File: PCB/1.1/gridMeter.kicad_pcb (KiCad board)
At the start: 2 copper layers, 50 x 50 mm, 26 parts, among them CON1 AC POWER, IC1 ATTINY84A-SS, P2 AC POWER, P3 MOTOR, P4 ISP, U1 LE33CZ-TR, U2 TCXO_SMD_4P, U3 TCRT5000, U4 7805, U5 ULN2003

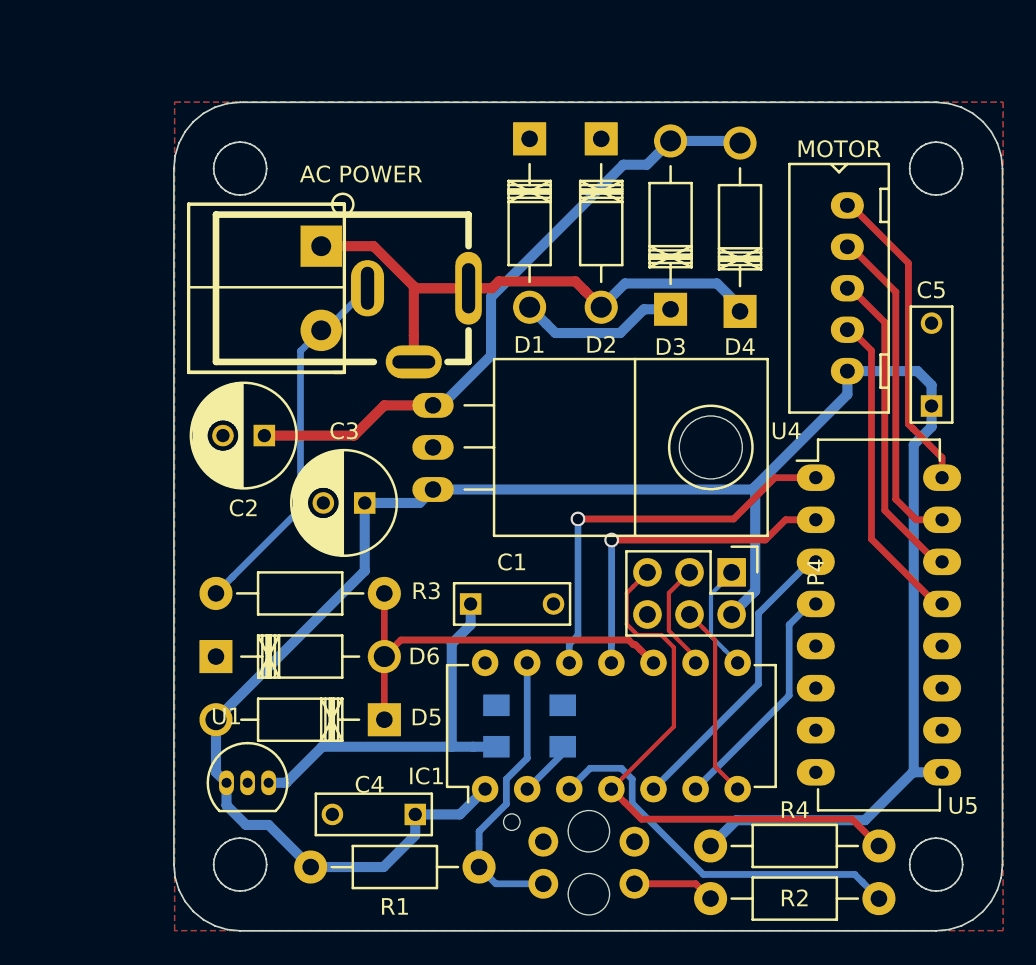
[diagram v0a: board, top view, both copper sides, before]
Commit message: Changes to Schematic PCB Gerbers
Matt Little changes to components - added different values and suppliers
codes. Slight change to PCB and footprints. Added Logo to silkscreen.
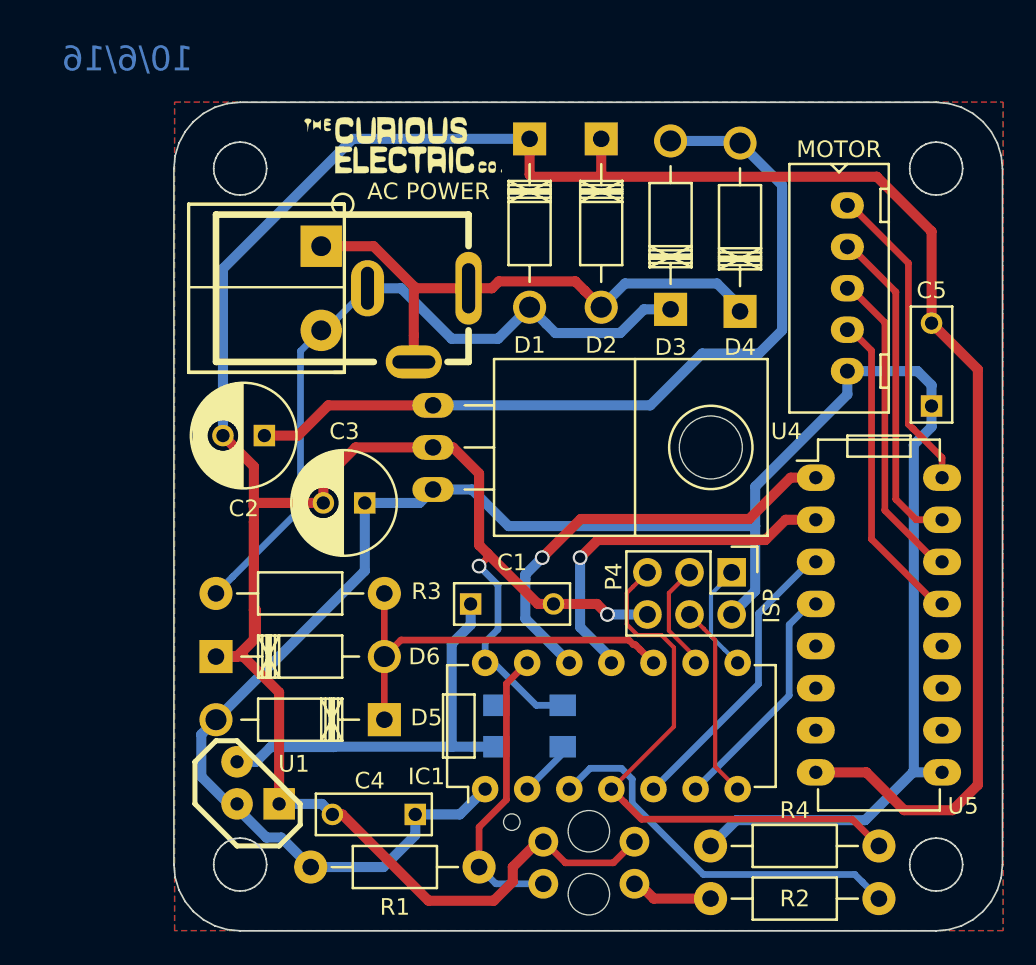
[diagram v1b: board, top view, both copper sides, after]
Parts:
- added P6: LOGO1, CuriousElectric2:CuriousElectric_flat_12mm, F.Cu at (193.7, 122.6)
- IC1: value ATTINY84A-SS -> ATTINY84A-PU; footprint Housings_DIP:DIP-14_W7.62mm -> DIP-14_W7.62mm
- U1: value LE33CZ-TR -> MCP170-3_3V; footprint TO_SOT_Packages_THT:TO-92_Inline_Narrow_Oval -> matts_components:TO92-MCP1700
- U5: footprint Housings_DIP:DIP-16_W7.62mm_LongPads -> DIP-16_W7.62mm_LongPads
- moved U1 1.91 mm to (185.0, 161.1), turned to 90 degrees
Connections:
- U2 pad 1: (no net) -> Net-(U2-Pad1)
- U5 pad 10: (no net) -> Net-(U5-Pad10)
- U5 pad 11: (no net) -> Net-(U5-Pad11)
- U5 pad 12: (no net) -> Net-(U5-Pad12)
- U5 pad 5: (no net) -> Net-(U5-Pad5)
- U5 pad 6: (no net) -> Net-(U5-Pad6)
- U5 pad 7: (no net) -> Net-(U5-Pad7)
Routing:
- net GND: track 0.00 -> 217.8 mm, vias 0 -> 2
- net Net-(C2-Pad1): track 38.2 -> 51.0 mm
- net /MAINSF: track 32.1 -> 43.9 mm
- net /IN2: track 20.2 -> 24.4 mm
- net /IN1: track 24.3 -> 26.4 mm
- net VCC: track 129.0 -> 130.6 mm
- net Net-(C1-Pad1): track 23.7 -> 25.1 mm
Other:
- net class Default: clearance 0.254 -> 0.127; trace_width 0.254 -> 0.6096
- rule trace_clearance: 0.254 -> 0.127
- board text added: "10/6/16"
- board text added: "Mains Frequency Meter v1.2"
- board text removed: "Mains Frequency Meter v1.1"

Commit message: Final changes before PCB run 1
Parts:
- moved D5 1.90 mm to (192.7, 155.4)
- moved D6 1.27 mm to (182.5, 152.2)
- moved U1 1.27 mm to (185.0, 159.8)
- moved R3 0.63 mm to (187.6, 149.0)
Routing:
- net GND: track 217.8 -> 207.5 mm
- net VCC: track 130.6 -> 137.4 mm
- net /DMAINSF: track 24.8 -> 23.3 mm
